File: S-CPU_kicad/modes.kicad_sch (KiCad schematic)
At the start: 13 parts

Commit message: Fix ERC errors in schematics.
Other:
- title: SNES S-CPU Schematics  -> Reverse Engineered SNES S-CPU Schematics 
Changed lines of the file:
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@@
   (paper "A4")
   (title_block
-    (title "SNES S-CPU Schematics ")
+    (title "Reverse Engineered SNES S-CPU Schematics ")
     (date "2023-10-21")
     (rev "0.1")

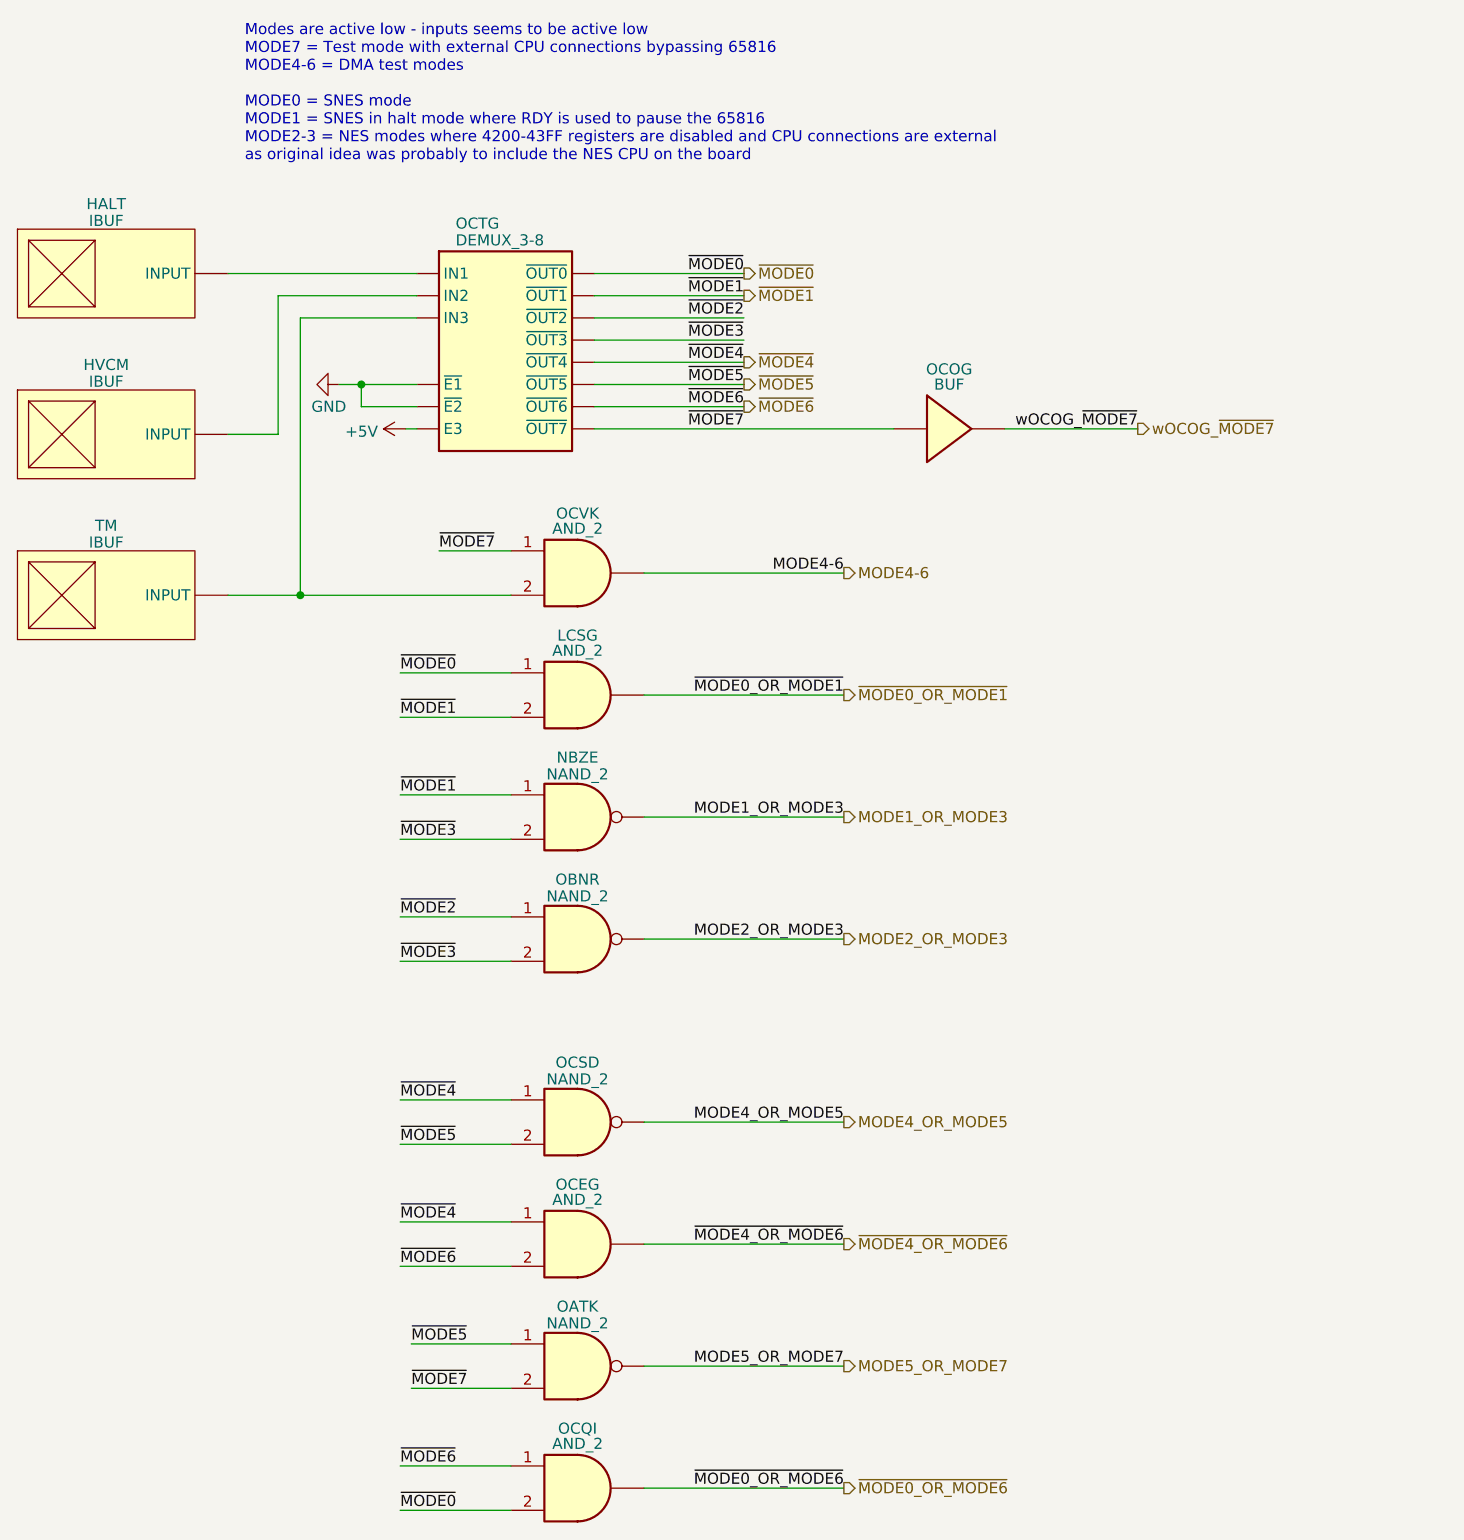
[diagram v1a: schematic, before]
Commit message: Big rework on the hierachical sheet to make thigs a bit clearer. PDF exported for Rev 0.1.
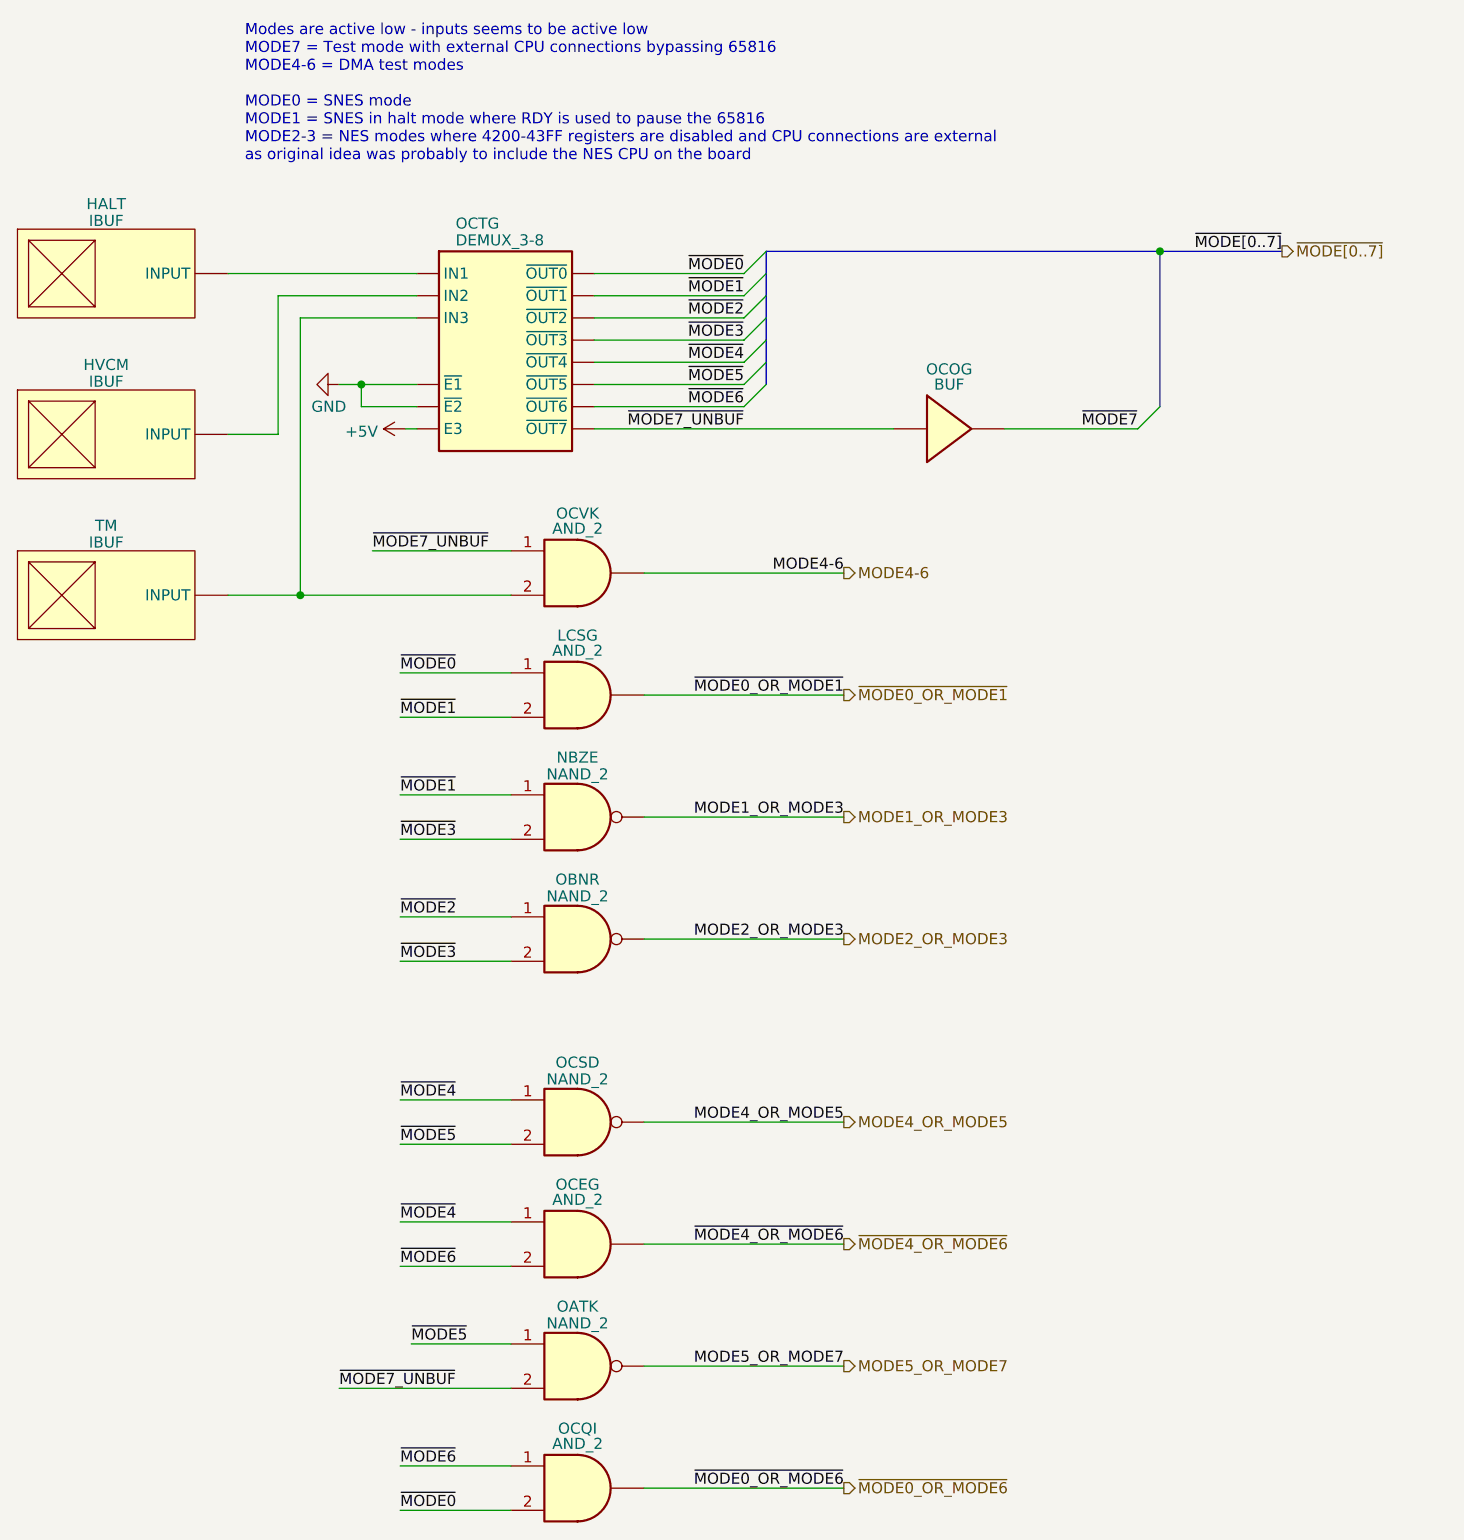
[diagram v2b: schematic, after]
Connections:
- net wOCOG_~{MODE7} is gone; now on net ~{MODE7}: OCOG.2
- net ~{MODE7}: no longer OATK.2, OCOG.1, OCTG. (~{OUT7}), OCVK.1
- new net ~{MODE7_UNBUF}: OATK.2, OCOG.1, OCTG. (~{OUT7}), OCVK.1

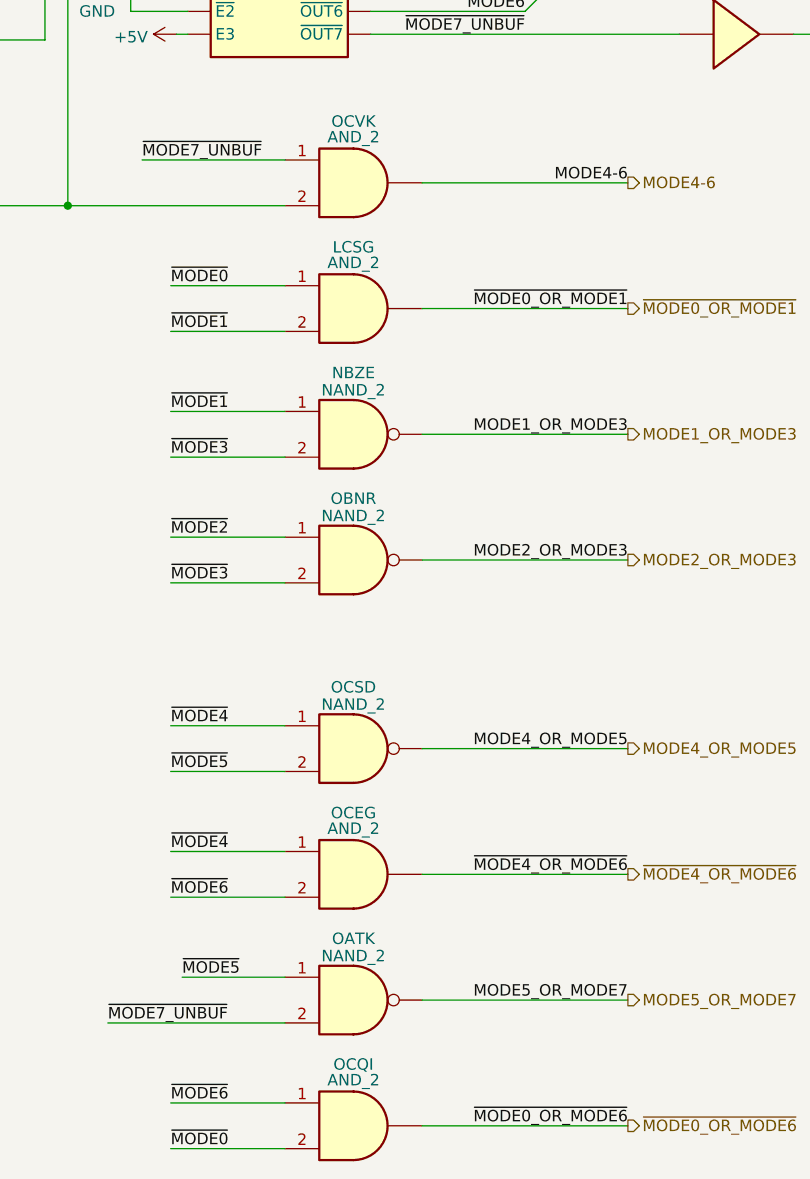
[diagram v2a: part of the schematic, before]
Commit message: Fixed VAWR which should have been an SR DFF (to fix issue #3 raised in github)
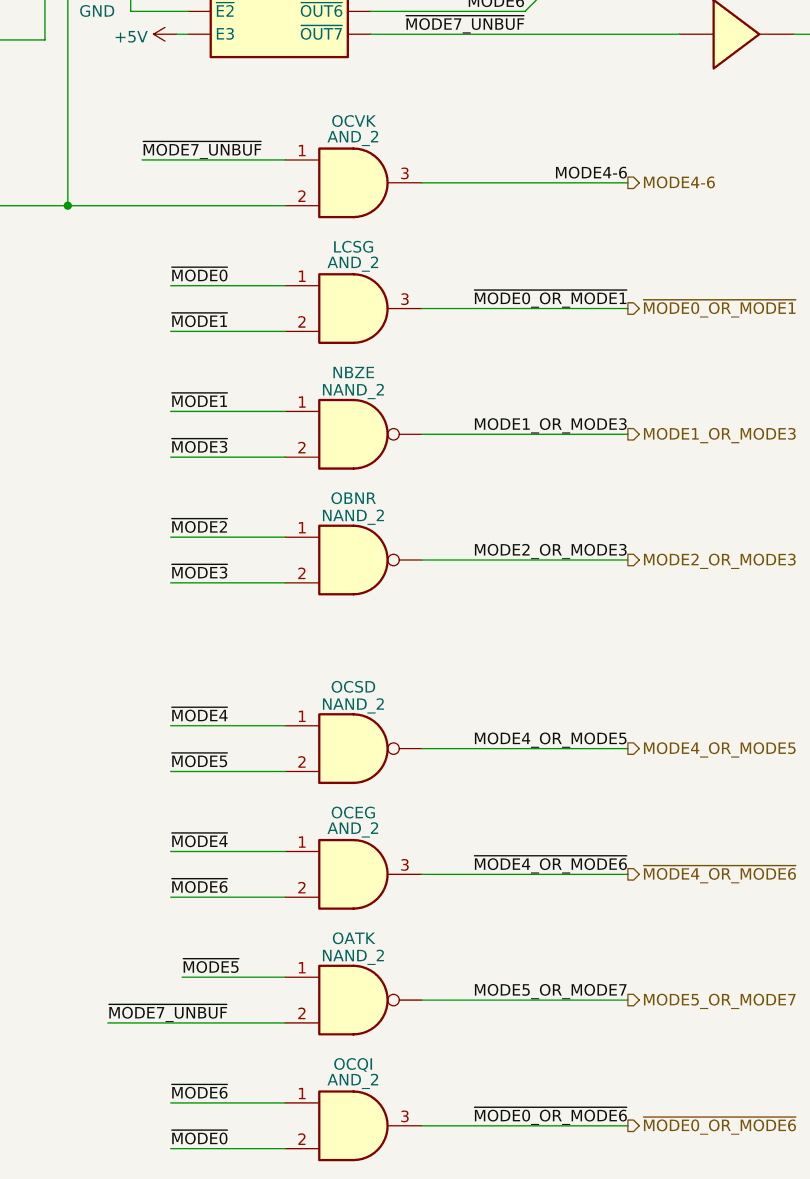
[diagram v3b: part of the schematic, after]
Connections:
- net +5V: now also OCTG.6 (E3); no longer OCTG. (~{OUT7})
- net GND: now also OCTG.4 (~{E1}), OCTG.5 (~{E2}); no longer OCTG. (~{OUT7})
- net ~{MODE0}: now also OCTG.7 (~{OUT0}); no longer OCTG. (~{OUT7})
- net ~{MODE1}: now also OCTG.8 (~{OUT1}); no longer OCTG. (~{OUT7})
- net ~{MODE2}: now also OCTG.9 (~{OUT2}); no longer OCTG. (~{OUT7})
- net ~{MODE3}: now also OCTG.10 (~{OUT3}); no longer OCTG. (~{OUT7})
- net ~{MODE4}: now also OCTG.11 (~{OUT4}); no longer OCTG. (~{OUT7})
- net ~{MODE5}: now also OCTG.12 (~{OUT5}); no longer OCTG. (~{OUT7})
- net ~{MODE6}: now also OCTG.13 (~{OUT6}); no longer OCTG. (~{OUT7})
- net ~{MODE7_UNBUF}: now also OCTG.15 (~{OUT7}); no longer OCTG. (~{OUT7})
- net at OCVK.2, TM.1 (INPUT): now also OCTG.3 (IN3); no longer OCTG. (~{OUT7})
- net at HALT.1 (INPUT): now also OCTG.1 (IN1); no longer OCTG. (~{OUT7})
- net at HVCM.1 (INPUT): now also OCTG.2 (IN2); no longer OCTG. (~{OUT7})
